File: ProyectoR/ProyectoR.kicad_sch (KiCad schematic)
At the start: 16 parts, among them J1 Conn_01x06, J2 Conn_01x04, Q1 BC547, Q2 BC547, Q3 BC547, Q4 BC547, SW1 SW_DIP_x01, SW2 SW_DIP_x01, U1 4N25, U2 Pico

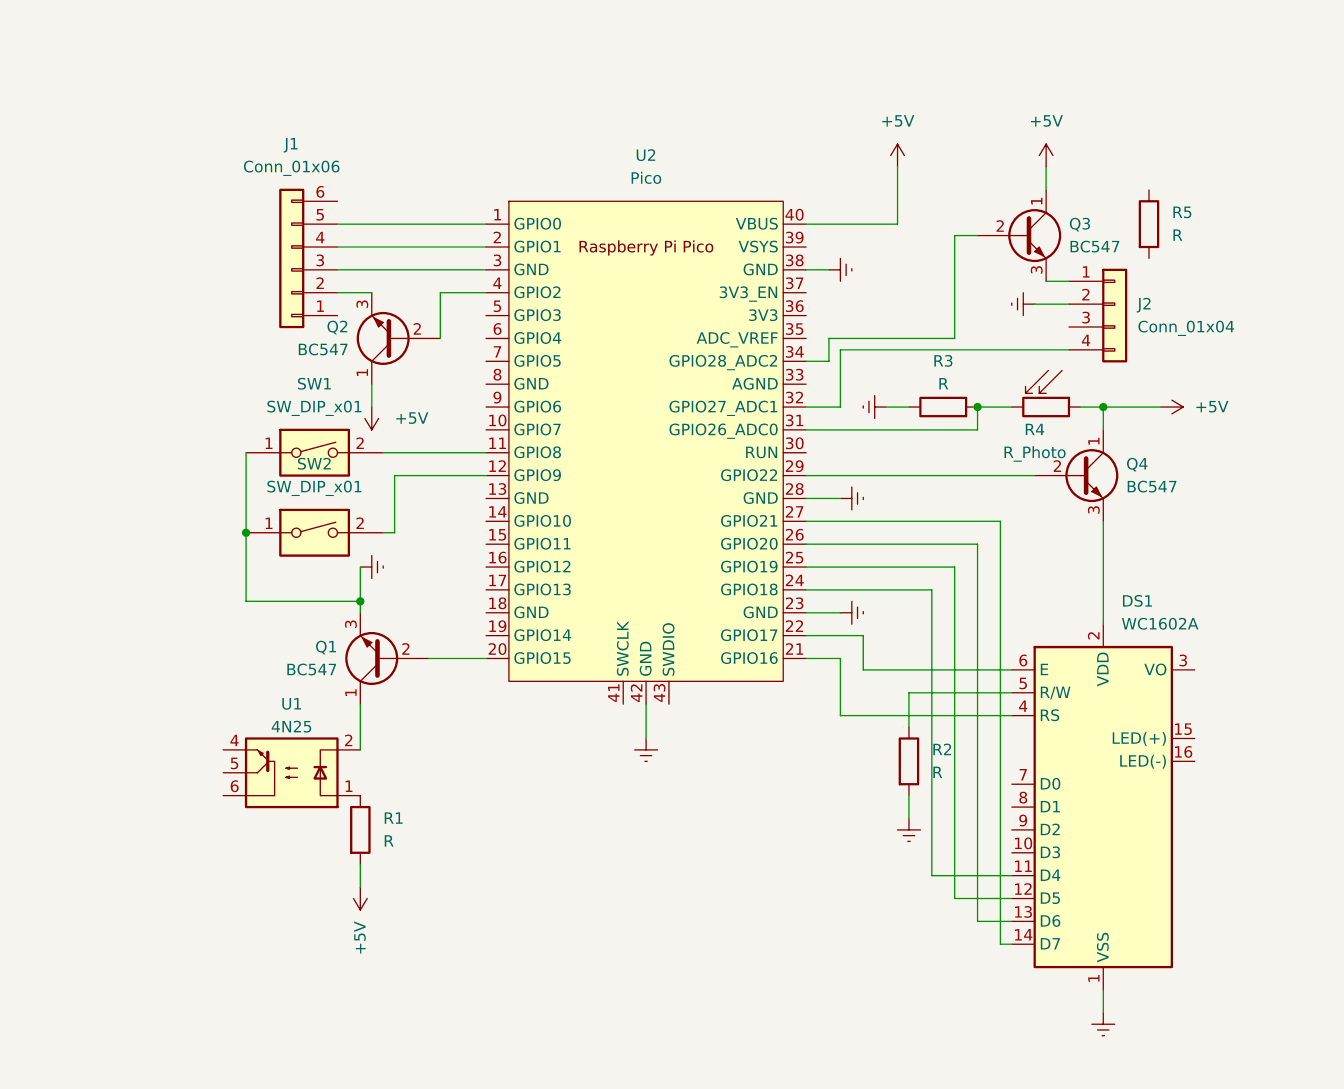
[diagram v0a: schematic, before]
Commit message: Falta terminar
Acomodé la librería de footprints, cambié tierras con GND, cambié fotoresistor por pin de 2.54mm entre otro
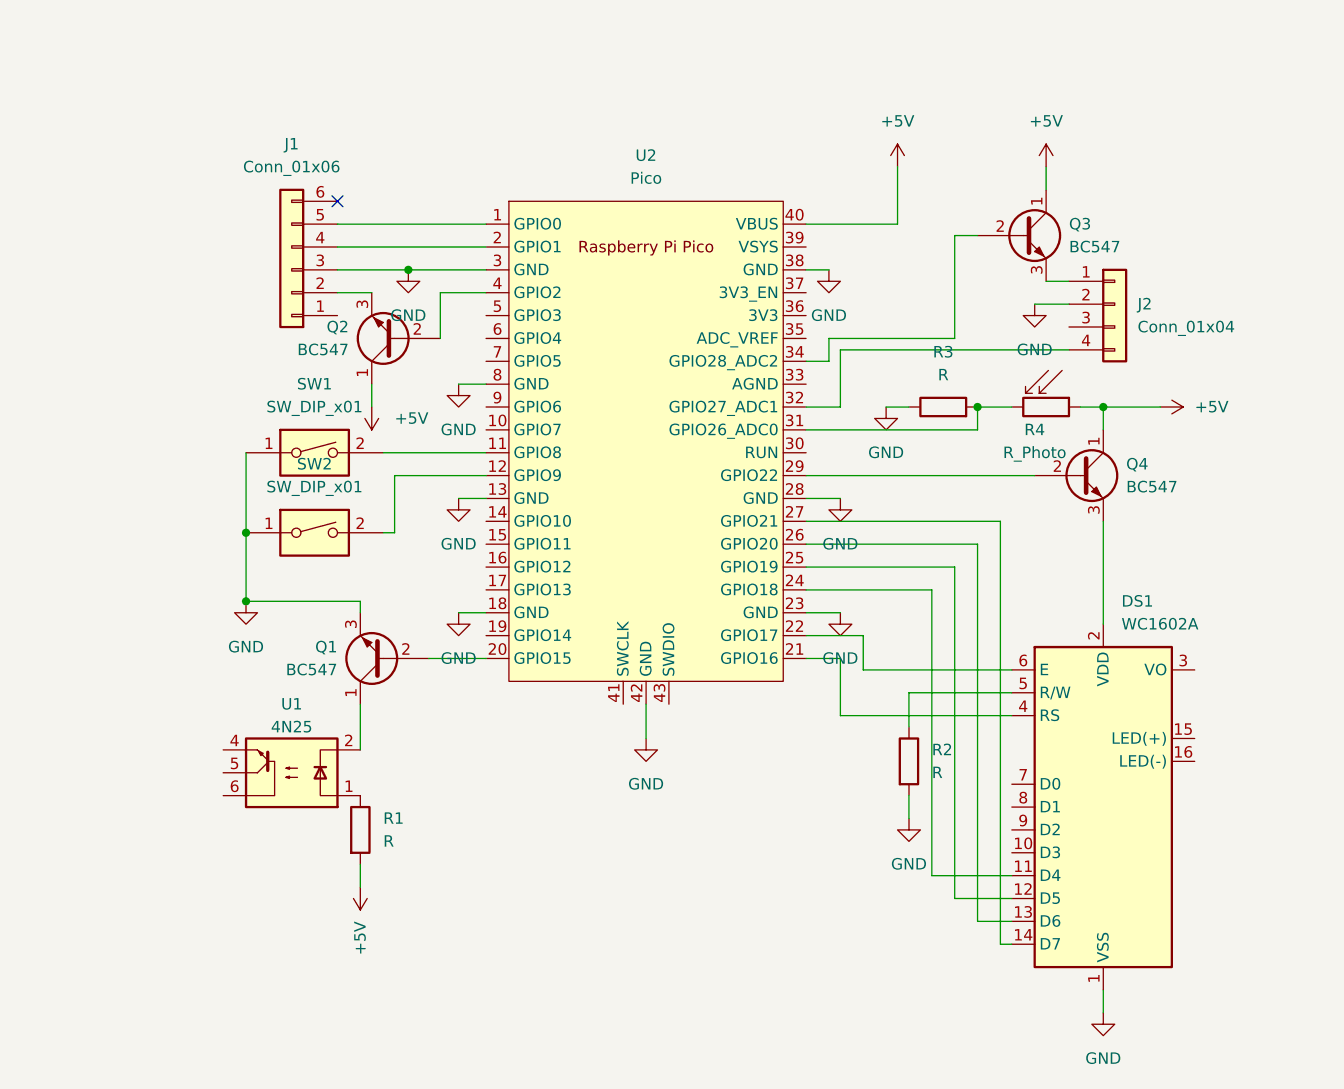
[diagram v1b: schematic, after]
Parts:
- removed R5: R, symbol Device:R
- J1: footprint (none) -> Connector_PinHeader_2.54mm:PinHeader_1x06_P2.54mm_Vertical
- J2: footprint (none) -> Connector_PinHeader_2.54mm:PinHeader_1x04_P2.54mm_Vertical
- R1, R2, R3: footprint (none) -> Resistor_THT:R_Axial_DIN0207_L6.3mm_D2.5mm_P10.16mm_Horizontal
- R4: footprint (none) -> Connector_PinHeader_2.54mm:PinHeader_1x02_P2.54mm_Vertical
- SW1, SW2: footprint (none) -> Button_Switch_THT:SW_PUSH_6mm_H5mm
- U2: footprint RPi_Pico:RPi_Pico_SMD_TH -> Librerias kicad:RPi_Pico_SMD_TH
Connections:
- net Earth is gone; now on net GND: DS1.1 (VSS), J2.2 (Pin_2), Q1.3 (E), R2.2, R3.1, SW1.1, SW2.1, U2.23 (GND), U2.28 (GND), U2.38 (GND), U2.42 (GND)
- net GND: now reaches J1.3 (Pin_3), U2.3 (GND)
- net GND: now also U2.13 (GND), U2.18 (GND), U2.8 (GND)
- no-connect marks 0 -> 1

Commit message: V1.0.0
Terminé el pcb, quedó con tres puentes nomás
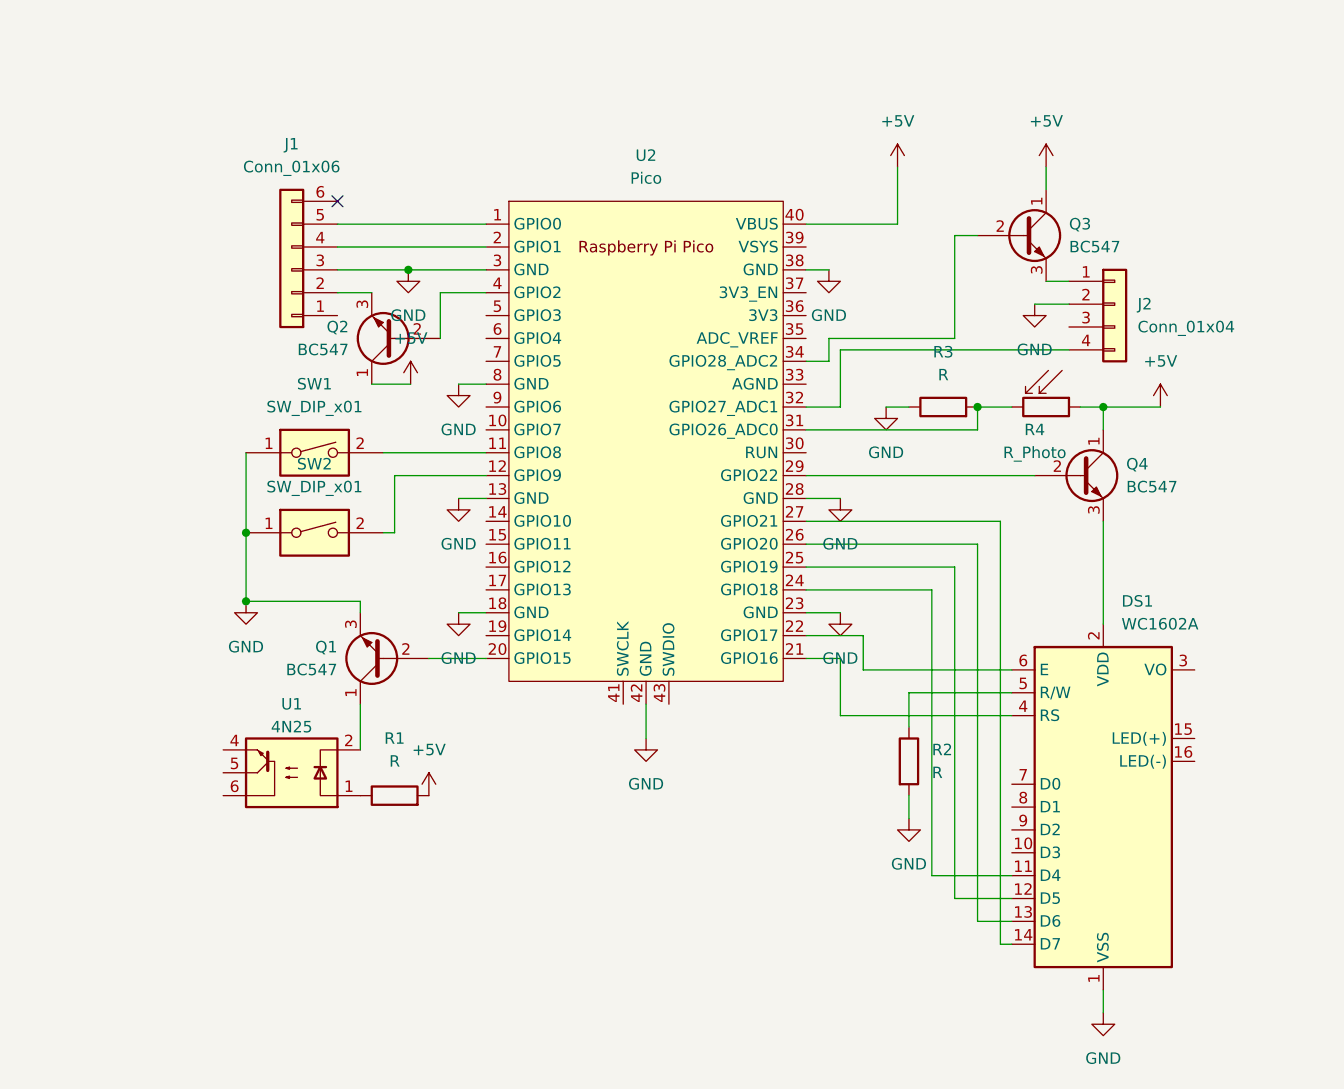
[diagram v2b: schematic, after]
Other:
- moved on the sheet: R1

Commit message: Add files via upload
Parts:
- removed U1: 4N25, Package_DIP:DIP-6_W7.62mm, symbol Isolator:4N25
- added J3: Screw_Terminal_01x02, symbol Connector:Screw_Terminal_01x02
- added J4: Screw_Terminal_01x02, TerminalBlock_Philmore:TerminalBlock_Philmore_TB132_1x02_P5.00mm_Horizontal, symbol Connector:Screw_Terminal_01x02
- added U1: MOC3023M, Package_DIP:DIP-6_W7.62mm, symbol Relay_SolidState:MOC3023M
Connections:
- net +5V: now also J3.1 (Pin_1)
- net GND: now also DS1.5 (R/W), J3.2 (Pin_2)
- net at Q2.2 (B): now also U2.20 (GPIO15); no longer U2.4 (GPIO2)
- net at R1.1: now also U1.1
- net at Q1.1 (C): now also U1.2
- net at SW2.2: now also U2.9 (GPIO6); no longer U2.12 (GPIO9)
- net at DS1.3 (VO): now also R2.1
- net at Q1.2 (B): now also U2.12 (GPIO9); no longer U2.20 (GPIO15)
- net at SW1.2: now also U2.5 (GPIO3); no longer U2.11 (GPIO8)
- new net: J4.2 (Pin_2), U1.4
- new net: J4.1 (Pin_1), U1.6
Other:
- moved on the sheet: R2, SW1, SW2
